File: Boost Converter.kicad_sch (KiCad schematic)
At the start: 37 parts, among them IC2 UCC5304DWVR, J3 Conn_01x01_Pin, J4 Conn_01x01_Pin, J5 Conn_01x01_Pin, J6 Conn_01x01_Pin, J7 Conn_01x01_Pin, J8 Conn_01x01_Pin, Q1 STB11NK50ZT4, U1 Nucleo_L432KC

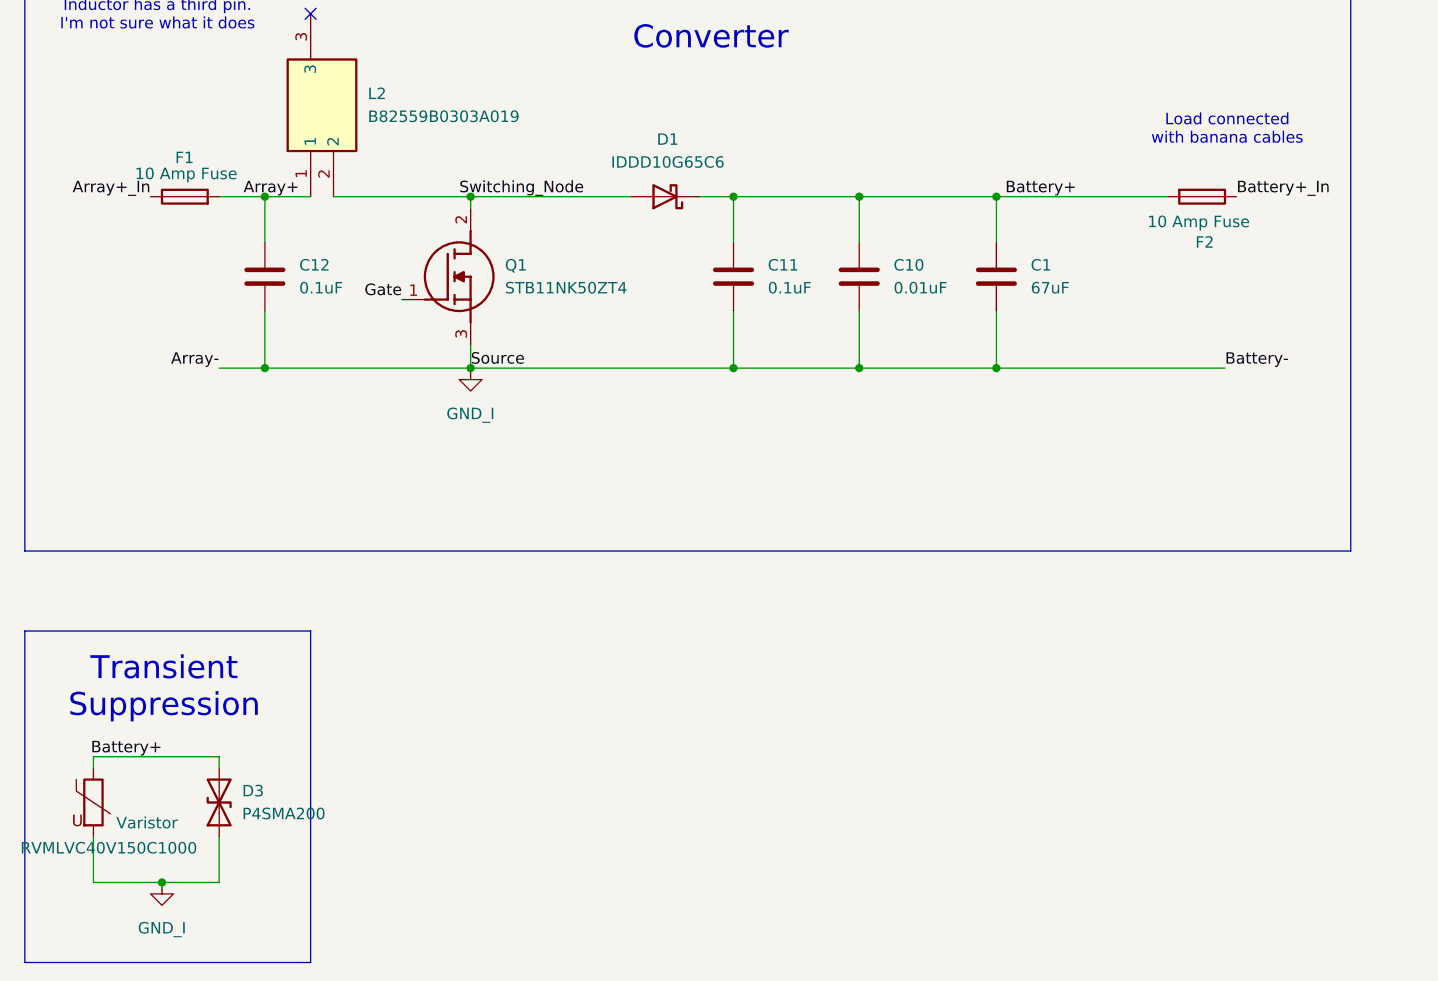
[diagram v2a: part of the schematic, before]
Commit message: New TVS diode, changed most traces to planes, added heatsink and thermal vias on mosfet. Made small adjustments to improve critical loop. Reworked some areas to shrink the board a little.
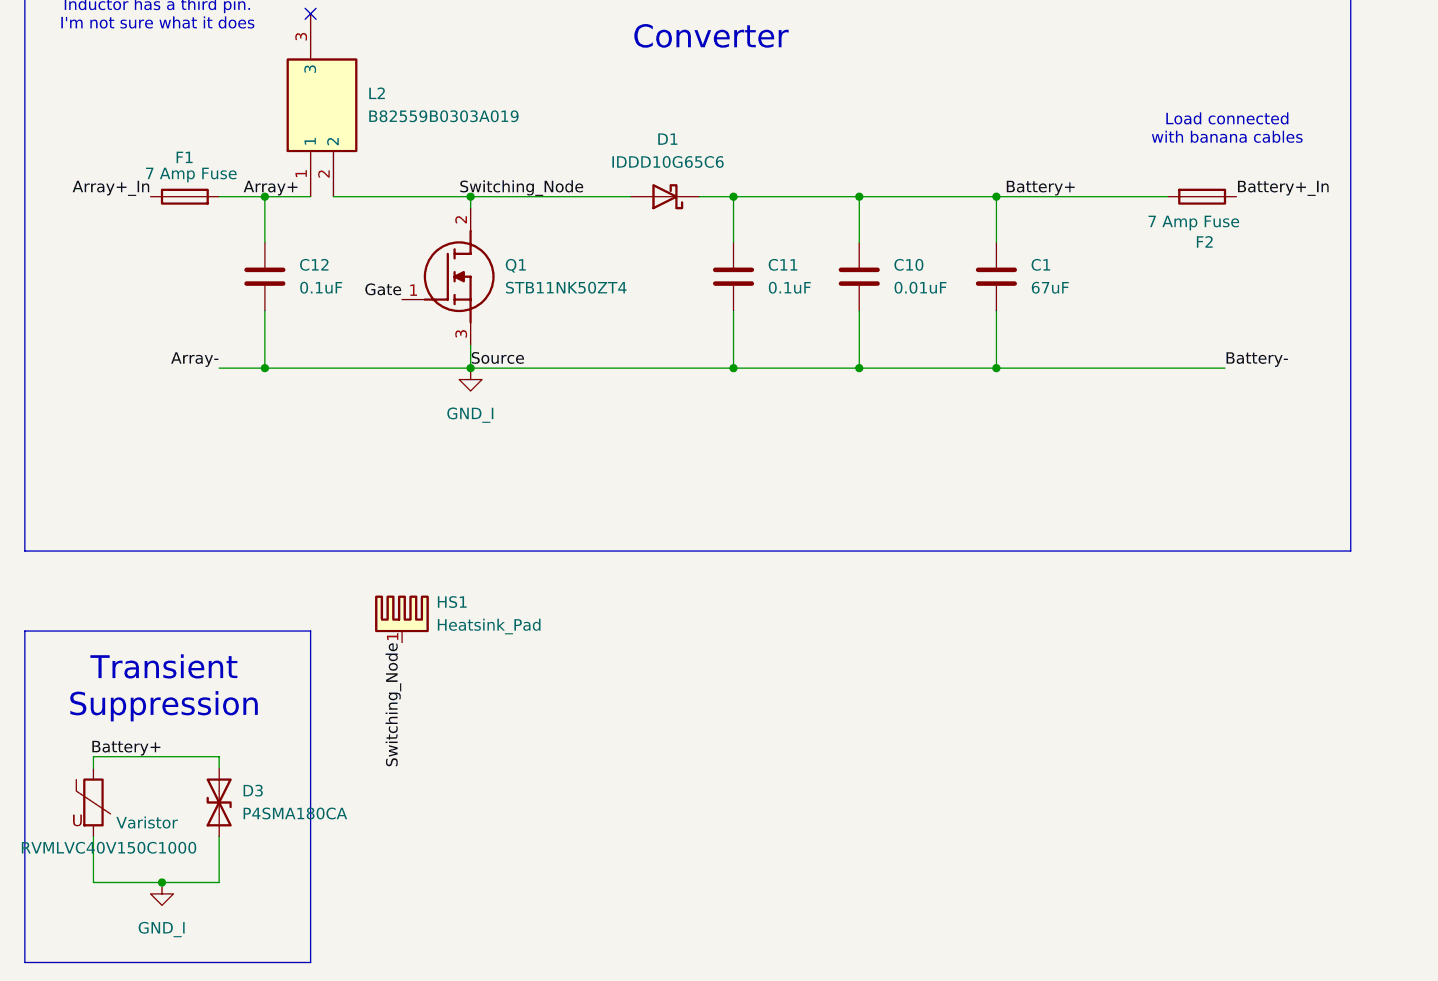
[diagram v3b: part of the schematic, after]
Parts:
- added HS1: Heatsink_Pad, symbol Mechanical:Heatsink_Pad
- D3: value P4SMA200 -> P4SMA180CA
- F1, F2: value 10 Amp Fuse -> 7 Amp Fuse
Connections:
- net Switching_Node: now also HS1.1
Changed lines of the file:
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@@
+		)
+	)
+	(label "Switching_Node"
+		(at 57.15 153.67 270)
+		(effects
+			(font
+				(size 1.27 1.27)
+			)
+			(justify right bottom)
 		)
 	)
@@
 			)
 		)
-		(property "Value" "10 Amp Fuse"
+		(property "Value" "7 Amp Fuse"
 			(at 38.862 101.6 90)
 			(effects
@@
 			)
 		)
-		(property "Value" "P4SMA200"
+		(property "Value" "P4SMA180CA"
 			(at 39.37 172.7199 90)
 			(effects
@@
 	)
 	(symbol
+		(lib_id "Mechanical:Heatsink_Pad")
+		(at 57.15 151.13 0)
+		(unit 1)
+		(exclude_from_sim no)
+		(in_bom yes)
+		(on_board yes)
+		(dnp no)
+		(fields_autoplaced yes)
+		(property "Reference" "HS1"
+			(at 60.96 149.2249 0)
+			(effects
+				(font
+					(size 1.27 1.27)
+				)
+				(justify left)
+			)
+		)
+		(property "Value" "Heatsink_Pad"
+			(at 60.96 151.7649 0)
+			(effects
+				(font
+					(size 1.27 1.27)
+				)
+				(justify left)
+			)
+		)
+		(property "Footprint" ""
+			(at 57.4548 152.4 0)
+			(effects
+				(font
+					(size 1.27 1.27)
+				)
+				(hide yes)
+			)
+		)
+		(property "Datasheet" "~"
+			(at 57.4548 152.4 0)
+			(effects
+				(font
+					(size 1.27 1.27)
+				)
+				(hide yes)
+			)
+		)
+		(property "Description" "Heatsink with electrical connection, 1 pin"
+			(at 57.15 151.13 0)
+			(effects
+				(font
+					(size 1.27 1.27)
+				)
+				(hide yes)
+			)
+		)
+		(pin "1"
+		)
+		(instances
+			(project ""
+				(path "/b493c70f-af76-4849-8864-15c5ad23cc75"
+					(reference "HS1")
+					(unit 1)
+				)
+			)
+		)
+	)
+	(symbol
 		(lib_id "Device:Fuse")
 		(at 146.05 104.14 270)
@@
 			)
 		)
-		(property "Value" "10 Amp Fuse"
+		(property "Value" "7 Amp Fuse"
 			(at 139.954 106.934 90)
 			(effects
